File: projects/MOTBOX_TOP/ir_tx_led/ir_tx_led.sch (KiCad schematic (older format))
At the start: 2 parts, among them J1 Conn_01x02

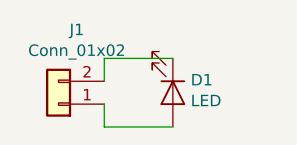
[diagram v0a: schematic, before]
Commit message: New library files and schematics with ESE31 and DT045 switches
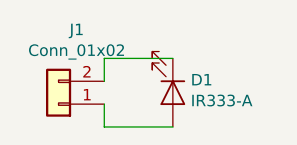
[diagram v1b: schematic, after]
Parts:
- D1: value LED -> IR333-A
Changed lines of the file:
@@
 P 4850 2800
 F 0 "D1" V 4795 2878 50  0000 L CNN
-F 1 "LED" V 4886 2878 50  0000 L CNN
+F 1 "IR333-A" V 4886 2878 50  0000 L CNN
 F 2 "LED_THT:LED_D5.0mm_Horizontal_O6.35mm_Z9.0mm" H 4850 2800 50  0001 C CNN
 F 3 "~" H 4850 2800 50  0001 C CNN
